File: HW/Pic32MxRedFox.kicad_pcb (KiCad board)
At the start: 2 copper layers, 20.3 x 59.7 mm, 39 parts, among them J1 USB_C_Receptacle_USB2.0, J2 Conn_02x05_Odd_Even, J3 Conn_01x20, J4 Conn_01x20, SW1 SW_Push, SW2 SW_Push, U2 LN1134A332MR-G, U3 SRV05-4, U4 PIC32MX270F256D-IPT, Y1 Crystal_GND2, Y2 Crystal

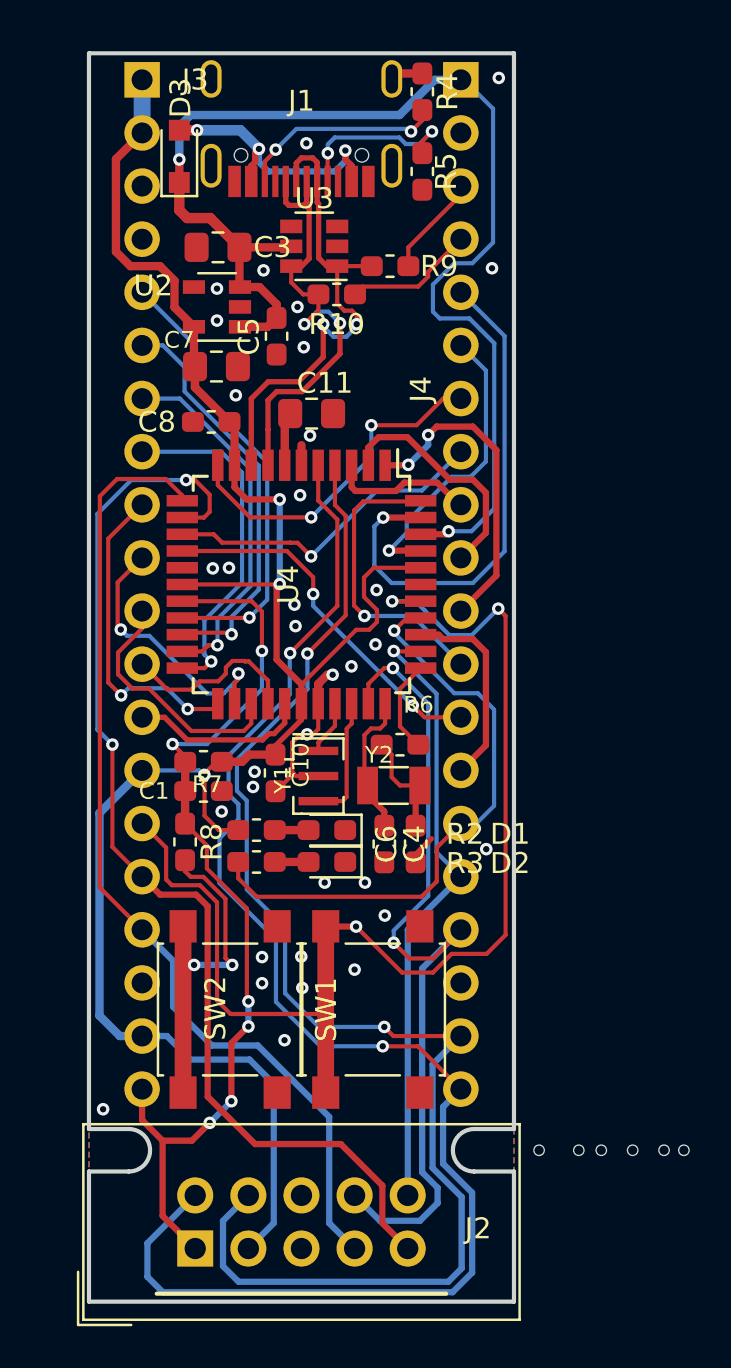
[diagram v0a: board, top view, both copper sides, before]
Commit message: New revision that actually fits in a DIP40 socket. Pinout stays the same.
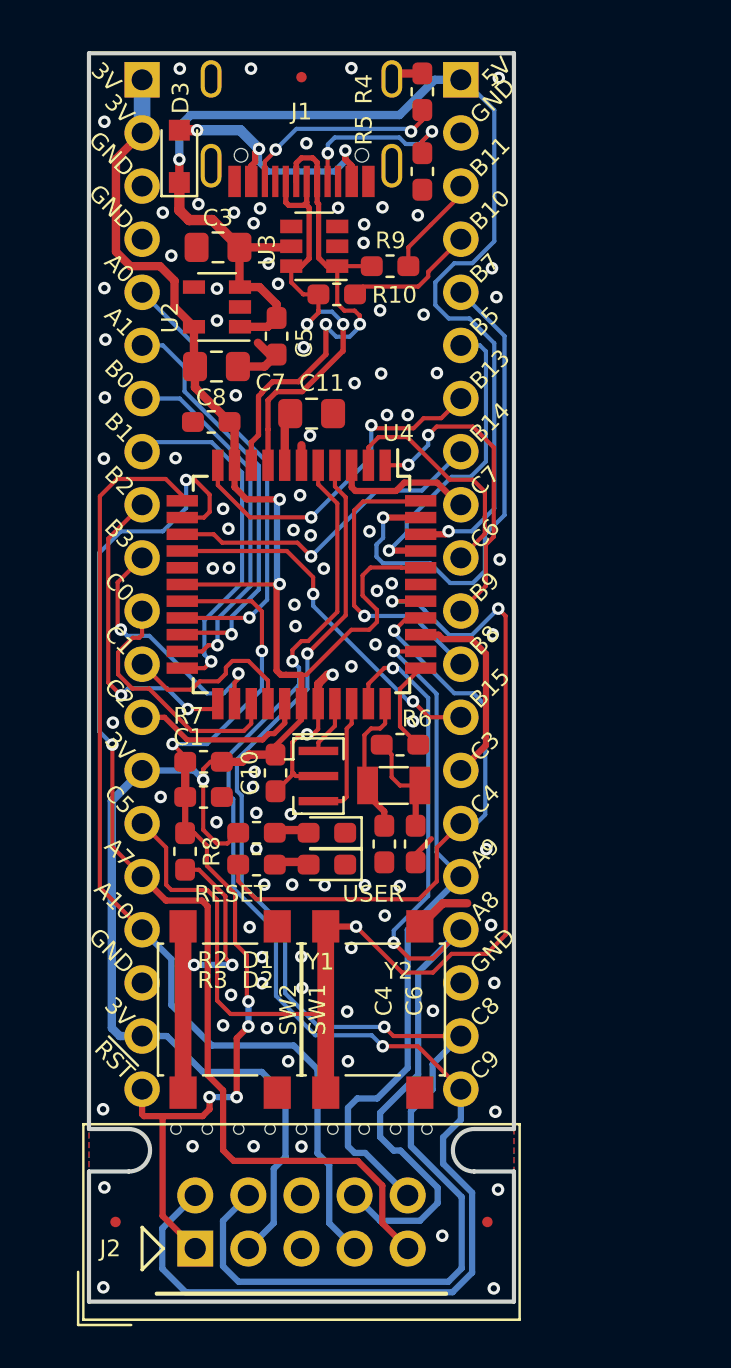
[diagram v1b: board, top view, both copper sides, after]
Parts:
- added FID1: Fiducial, Fiducial:Fiducial_0.5mm_Mask1mm, F.Cu at (110.5, 91.3)
- added FID2: Fiducial, Fiducial:Fiducial_0.5mm_Mask1mm, F.Cu at (101.6, 146.1)
- added FID3: Fiducial, Fiducial:Fiducial_0.5mm_Mask1mm, F.Cu at (119.4, 146.1)
- added H7: MB_0.5, KiCAD library:MouseBiteHole_0.5mm, F.Cu at (113.5, 141.6)
- added H8: MB_0.5, KiCAD library:MouseBiteHole_0.5mm, F.Cu at (115.0, 141.6)
- added H9: MB_0.5, KiCAD library:MouseBiteHole_0.5mm, F.Cu at (116.5, 141.6)
- added MARK2: Logo_Open_Hardware_Small, Symbol:OSHW-Logo_5.7x6mm_SilkScreen, B.Cu at (109.9, 121.3)
- MARK1: moved to B.Cu
- R2, R3: value 1k -> 10k
- moved MARK1 30.1 mm to (110.1, 100.1), turned to 180 degrees
- moved H2 17.8 mm to (106.0, 141.6)
- moved H5 17.4 mm to (104.5, 141.6)
- moved H1 17.4 mm to (107.5, 141.6)
- moved H3 17.4 mm to (109.0, 141.6)
- moved H6 17.4 mm to (110.5, 141.6)
- moved H4 16.8 mm to (112.0, 141.6)
- moved R8 0.45 mm to (104.9, 128.3)
- moved C1 0.28 mm to (105.8, 125.7)
- moved D2 0.13 mm to (111.7, 129.0)
- moved R3 0.13 mm to (108.3, 129.0)
- moved D1 0.13 mm to (111.7, 127.4)
- moved R2 0.13 mm to (108.3, 127.4)
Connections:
- J1 pad A8: (no net) -> Net-(J1-PadA8)
- J1 pad B8: (no net) -> Net-(J1-PadB8)
- U2 pad 4: (no net) -> Net-(U2-Pad4)
- U3 pad 4: (no net) -> Net-(U3-Pad4)
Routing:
- net GND: track 12.5 -> 18.4 mm, vias 34 -> 98
- net /TDI: track 29.7 -> 32.9 mm
- net /TDO: track 40.0 -> 42.0 mm
- net +3V3: track 95.0 -> 96.8 mm
- net /UART2_TX: track 71.2 -> 69.5 mm
- net /~RESET~: track 44.8 -> 45.8 mm
- net /TMS/PGED4: track 47.2 -> 48.2 mm
- net /UART2_RX: track 65.9 -> 66.8 mm
- net /TCK/PGEC4: track 53.3 -> 53.9 mm
- net /SDI1: track 14.3 -> 14.8 mm
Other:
- rule pad_to_mask_clearance: 0.051 -> 0
- board text added: "3V"
- board text added: "5V"
- board text added: "A0"
- board text added: "A1"
- board text added: "A10"
- board text added: "A7"
- board text added: "A8"
- board text added: "A9"
- board text added: "AN0"
- board text added: "AN1"
- board text added: "AN12"
- board text added: "AN2"
- board text added: "AN3"
- board text added: "AN4"
- board text added: "AN5"
- board text added: "AN6"
- board text added: "AN7"
- board text added: "AN8"
- board text added: "AN9"
- board text added: "B0"
- board text added: "B1"
- board text added: "B10"
- board text added: "B11"
- board text added: "B13"
- board text added: "B14"
- board text added: "B15"
- board text added: "B2"
- board text added: "B3"
- board text added: "B5"
- board text added: "B7"
- board text added: "B8"
- board text added: "B9"
- board text added: "BTN_U"
- board text added: "C0"
- board text added: "C1"
- board text added: "C2"
- board text added: "C3"
- board text added: "C4"
- board text added: "C5"
- board text added: "C6"
- board text added: "C7"
- board text added: "C8"
- board text added: "C9"
- board text added: "GND"
- board text added: "LED_U"
- board text added: "PGEC4"
- board text added: "PGED4"
- board text added: "RB10"
- board text added: "RB11"
- board text added: "RB7"
- board text added: "RESET"
- board text added: "Rev2"
- board text added: "SCK1"
- board text added: "SCL1"
- board text added: "SDA1"
- board text added: "SDI1"
- board text added: "SDO1"
- board text added: "TDI"
- board text added: "TDO"
- board text added: "UA1_R"
- board text added: "UA1_T"
- board text added: "UA2_R"
- board text added: "UA2_T"
- board text added: "USER"
- board text added: "~MCLR~"
- board text added: "~RST~"
- board text removed: "3v 3v G GND AN0 AN1 AN2 AN3 AN4 AN5 AN6 AN7 AN8 3v BTN_U PGEC4 PGED4 GND 3v ~MCLR~"
- board text removed: "5v GND RB11 RB10 RB7 SDI1 SDO1 SCK1 UA1_T UA1_R SDA1 SCL1 AN9 AN12 LED_U TDI TDO GND UA2_R UA2_T"
- board text removed: "Rev1"
